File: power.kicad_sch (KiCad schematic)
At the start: 30 parts, among them J5 Molex_Nano-Fit_1x2_105309-1202, Q1 AO3401A, SW1 SW_EG1218, U4 AP62301_TSOT, U6 MCP1700T-3302E_TT

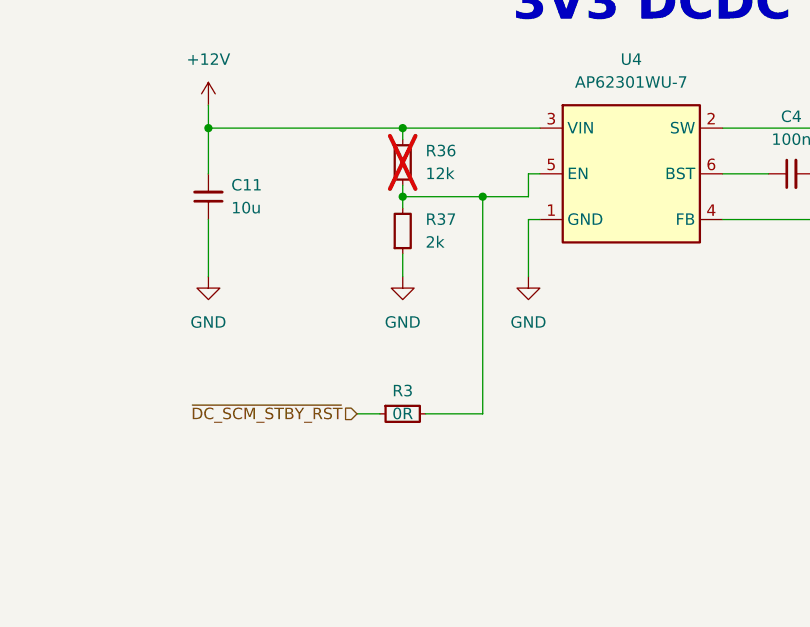
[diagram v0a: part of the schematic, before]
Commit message: [#93514] Leave one pull-down for DC_SCM_STBY_RST
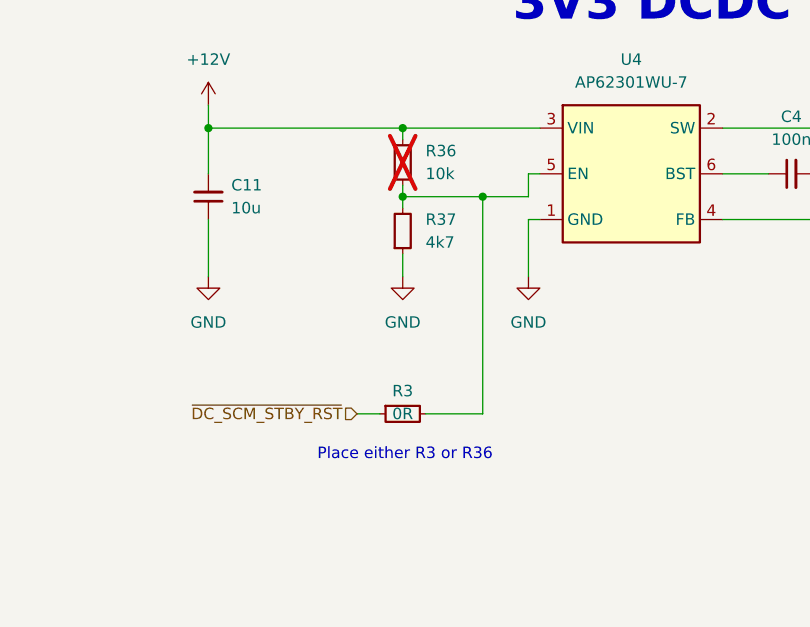
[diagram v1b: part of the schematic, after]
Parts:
- removed R36: R_12k_0402, antmicro-footprints:R_0402_1005Metric, symbol antmicroResistors0402:R_12k_0402
- removed R37: R_2k_0402, antmicro-footprints:R_0402_1005Metric, symbol antmicroResistors0402:R_2k_0402
- added R36: R_10k_0402, antmicro-footprints:R_0402_1005Metric, symbol antmicroResistors0402:R_10k_0402
- added R37: R_4k7_0402, antmicro-footprints:R_0402_1005Metric, symbol antmicroResistors0402:R_4k7_0402
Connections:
- net +12V: now also R36.2
- net GND: now also R37.1
- net at R3.2, U4.5 (EN): now also R36.1, R37.2
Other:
- note added: "Place either R3 or R36"

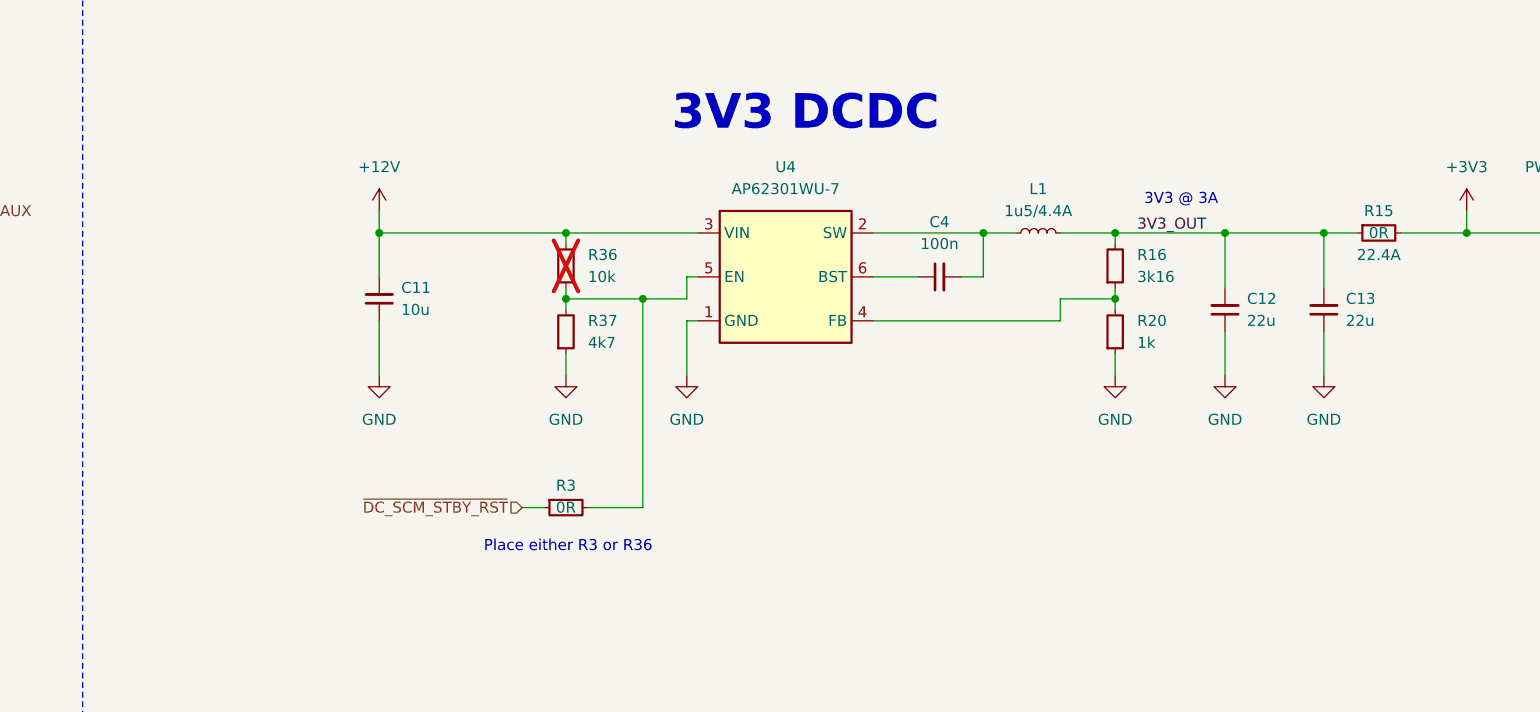
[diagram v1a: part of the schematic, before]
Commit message: [#93514] Add note for 3V3 power converter
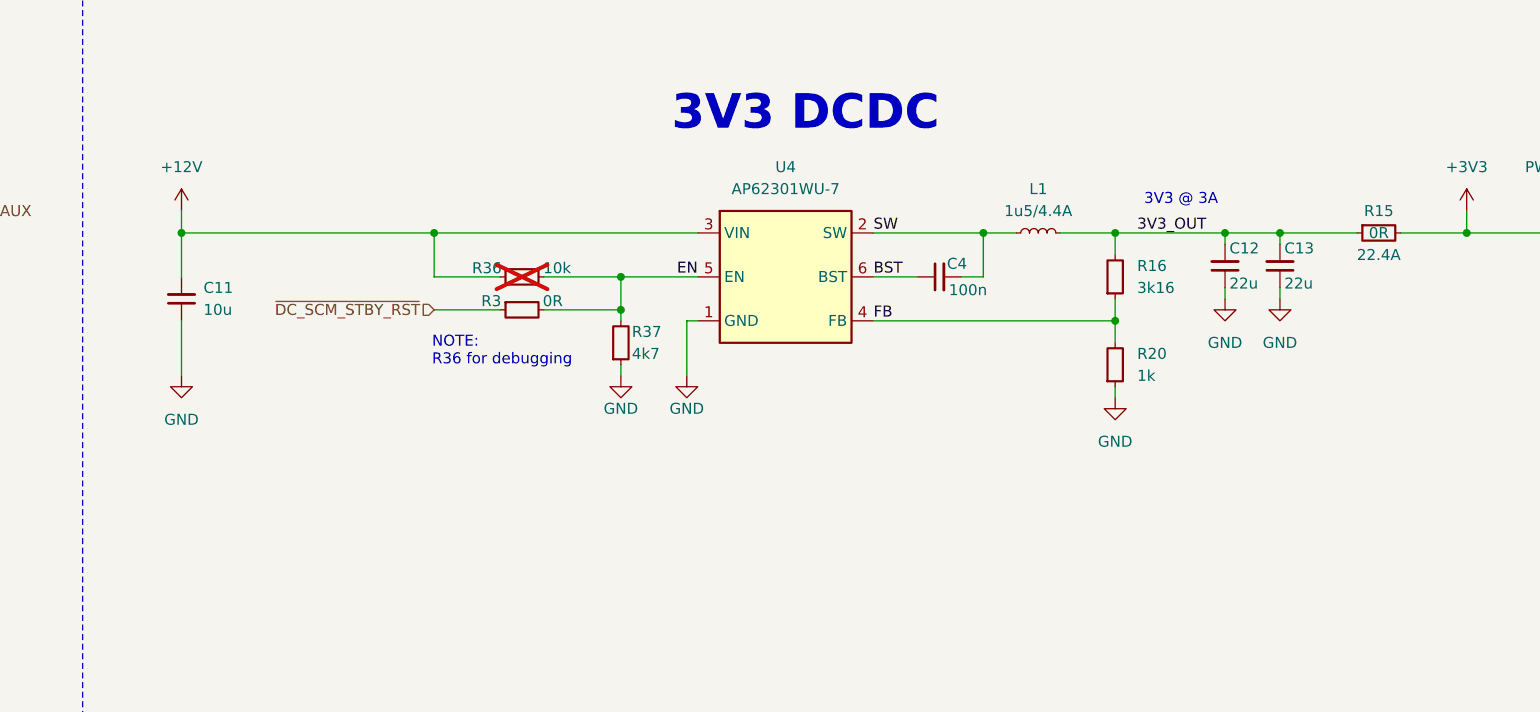
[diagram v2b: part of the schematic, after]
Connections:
- net SW: now reaches C4.2, L1.1, U4.2 (SW)
- net FB: now reaches R16.1, R20.2, U4.4 (FB)
- net EN: now reaches R3.2, R36.1, R37.2, U4.5 (EN)
- net BST: now reaches C4.1, U4.6 (BST)
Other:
- note added: "NOTE: R36 for debugging"
- note removed: "Place either R3 or R36"
- moved on the sheet: C11, C12, C13, R16, R20, R3, R36, R37

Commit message: [#93949] Change testpads to 1.5mm, change QSPI and UART testpad to smd technology
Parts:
- removed TP1, TP2, TP3, TP9: TP_0.75mm_SMD, antmicro-footprints:TP_SMD_0.75mm, symbol antmicroTestPoints:TP_0.75mm_SMD
- added TP1, TP2, TP3, TP9: TP_1.5mm_SMD, antmicro-footprints:TP_SMD_1.5mm, symbol antmicroTestPoints:TP_1.5mm_SMD
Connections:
- net +12V: now also TP1.1
- net +3V3: now also TP2.1
- net FTDI_3V3: now also TP3.1
- net GND: now also TP9.1

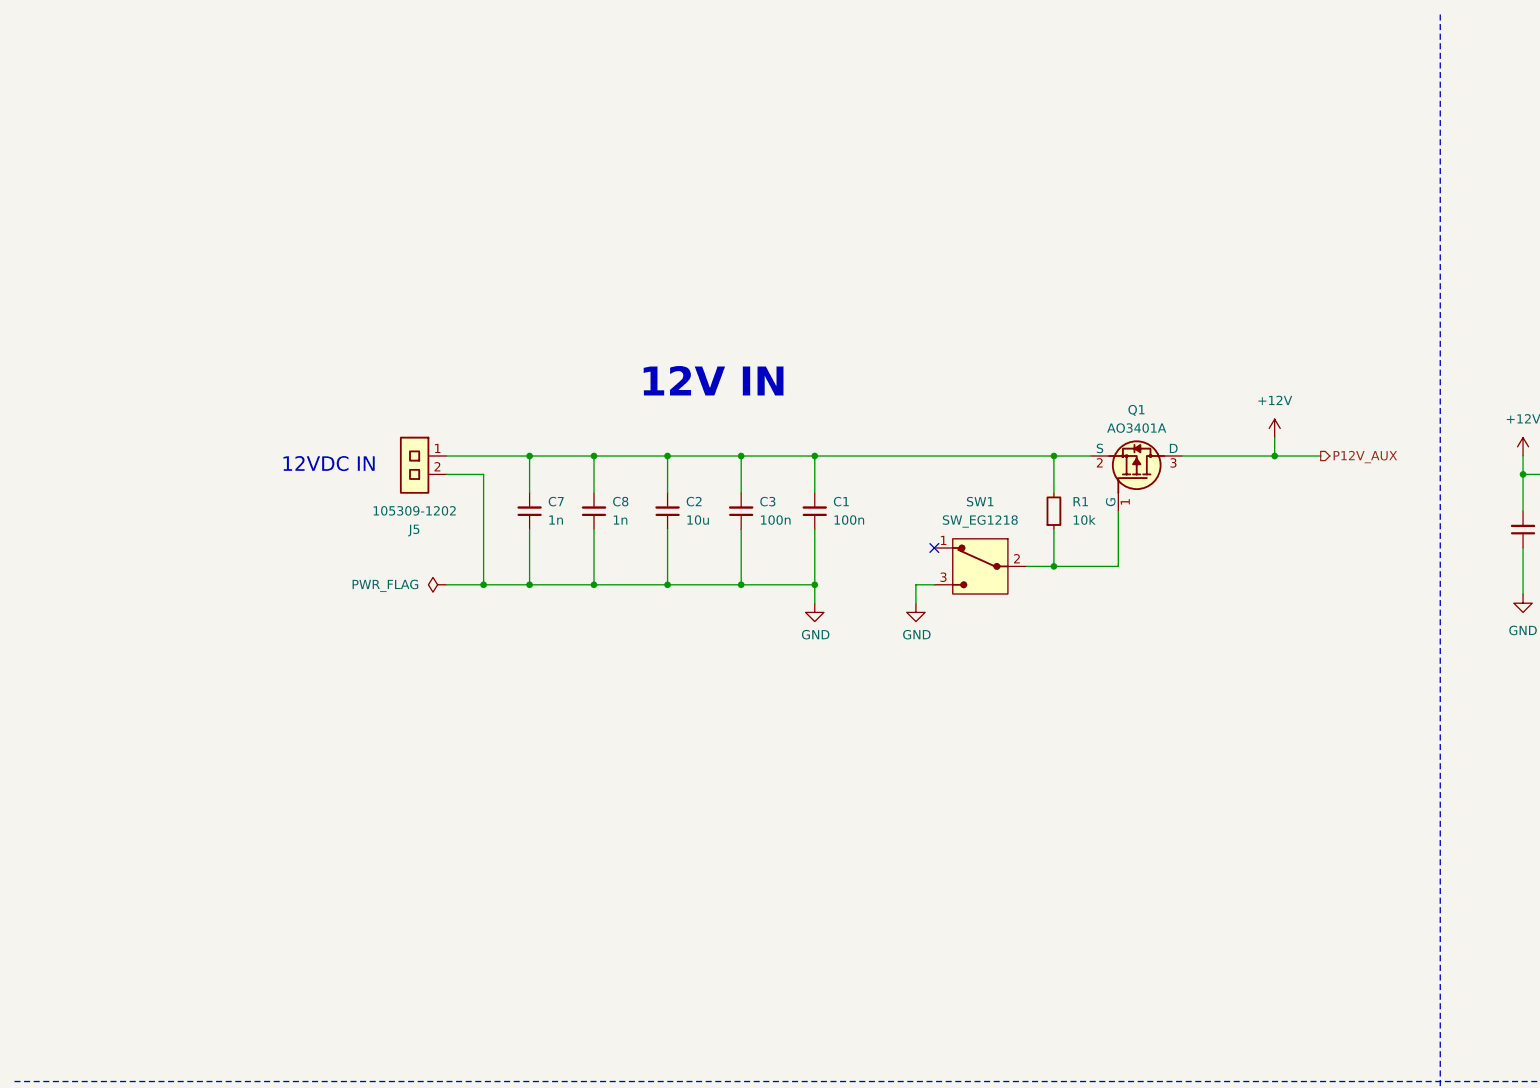
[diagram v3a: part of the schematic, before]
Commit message: [#93949] Add reverse voltage protection
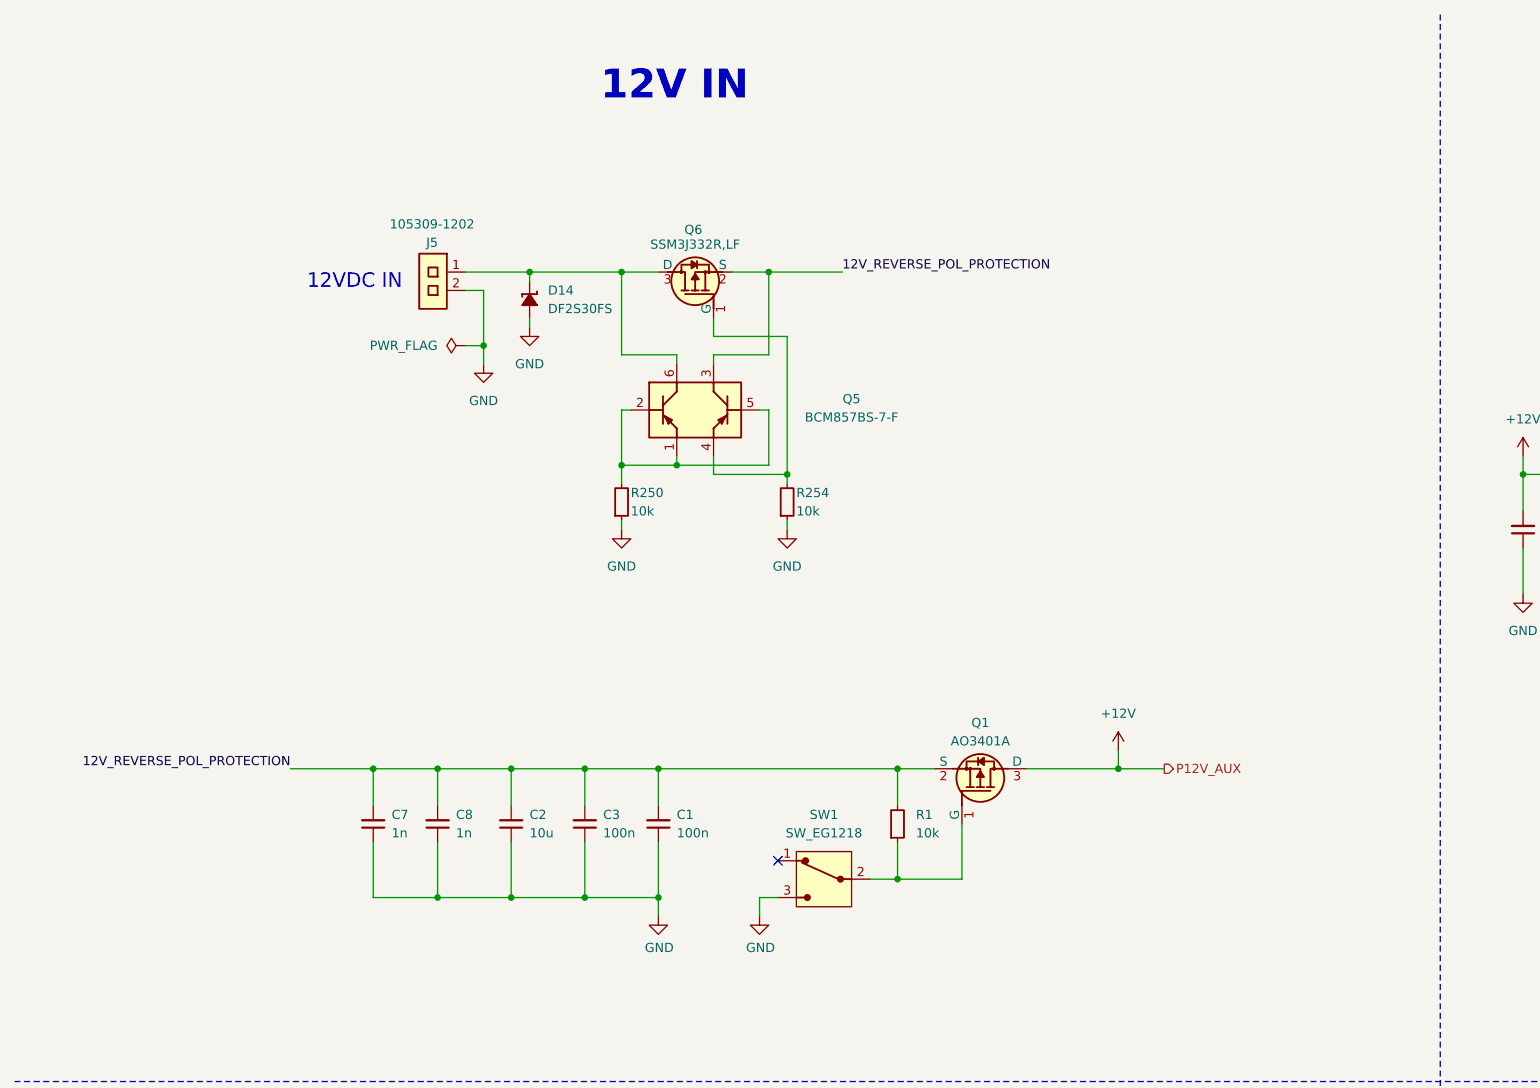
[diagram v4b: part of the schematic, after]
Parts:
- added D14: DF2S30FS_SOD, antmicro-footprints:SOD-923, symbol antmicroTVSDiodes:DF2S30FS_SOD
- added Q5: BCM857BS-7-F, antmicro-footprints:SOT-363, symbol antmicroTransistorsBipolarArrays:BCM857BS-7-F
- added Q6: SSM3J332R, antmicro-footprints:SOT-23-3, symbol antmicroTransistorsFETsMOSFETsSingle:SSM3J332R
- added R250, R254: R_10k_0402, antmicro-footprints:R_0402_1005Metric, symbol antmicroResistors0402:R_10k_0402
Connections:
- net GND: now also D14.2 (A), R250.1, R254.1
- net 12V_REVERSE_POL_PROTECTION: now reaches C1.2, C2.2, C3.2, C7.2, C8.2, Q1.2 (S), R1.2
- net 12V_REVERSE_POL_PROTECTION: now also Q5.3, Q6.2 (S); no longer J5.1
- new net: Q5.4, Q6.1 (G), R254.2
- new net: D14.1 (C), J5.1, Q5.6, Q6.3 (D)
- new net: Q5.1, Q5.2, Q5.5, R250.2
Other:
- moved on the sheet: C1, C2, C3, C7, C8, J5, Q1, R1, SW1

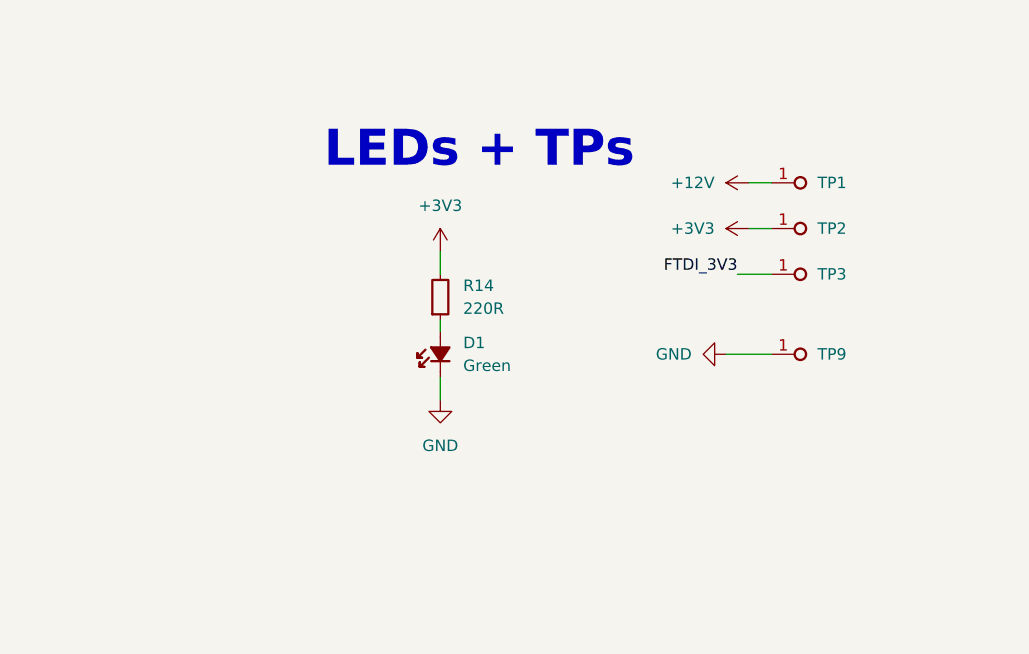
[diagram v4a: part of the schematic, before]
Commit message: [#93949] Add voltage LED indicators
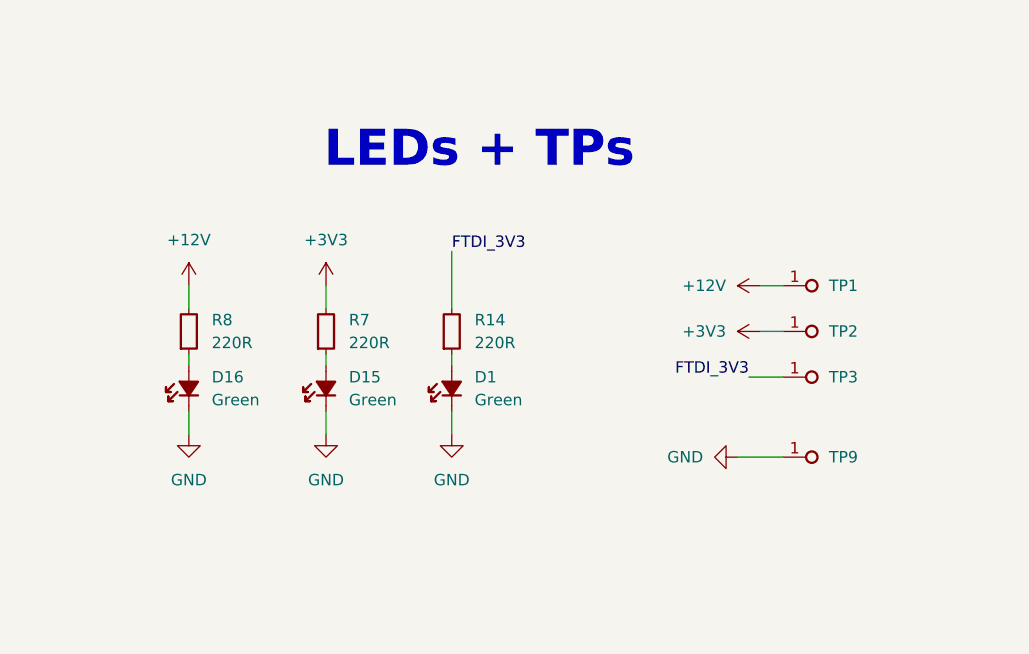
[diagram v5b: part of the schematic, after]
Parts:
- added D15, D16: LED_G_0402_VLMTG1500-GS08, antmicro-footprints:LED_0402_1005Metric_G, symbol antmicroLEDIndicationDiscrete:LED_G_0402_VLMTG1500-GS08
- added R7, R8: R_220R_0402, antmicro-footprints:R_0402_1005Metric, symbol antmicroResistors0402:R_220R_0402
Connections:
- net +12V: now also R8.2
- net +3V3: now also R7.2; no longer R14.2
- net FTDI_3V3: now also R14.2
- net GND: now also D15.1 (C), D16.1 (C)
- new net: D16.2 (A), R8.1
- new net: D15.2 (A), R7.1
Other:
- moved on the sheet: D1, R14, TP1, TP2, TP3, TP9
